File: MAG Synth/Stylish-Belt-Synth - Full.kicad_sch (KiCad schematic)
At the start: 39 parts, among them J0 USB_B, J1 Headphone, J26 WRITE PATCH, J27 PARAM SELECT, J28 PATCH SELECT, J29 MODE, J30 STYLUS, U1 stm32f103c8t6-module-china, U2 XPT8871

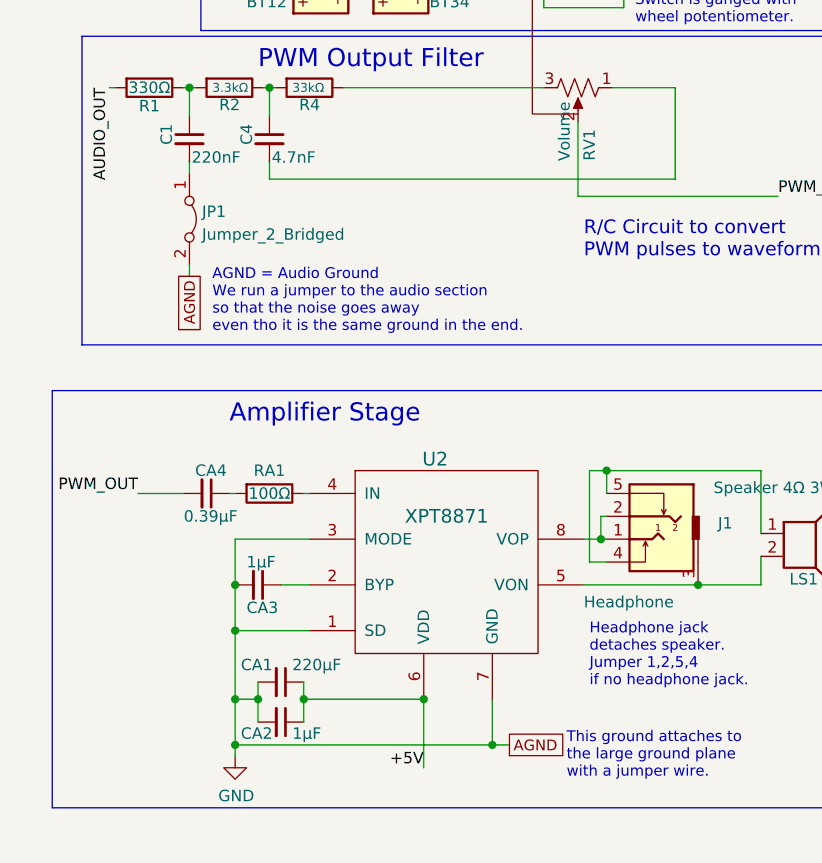
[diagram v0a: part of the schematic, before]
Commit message: Updated fix for audio problems, adds AGND to C4 too. 3d models for parts extracted from old PCB model - only partly complete
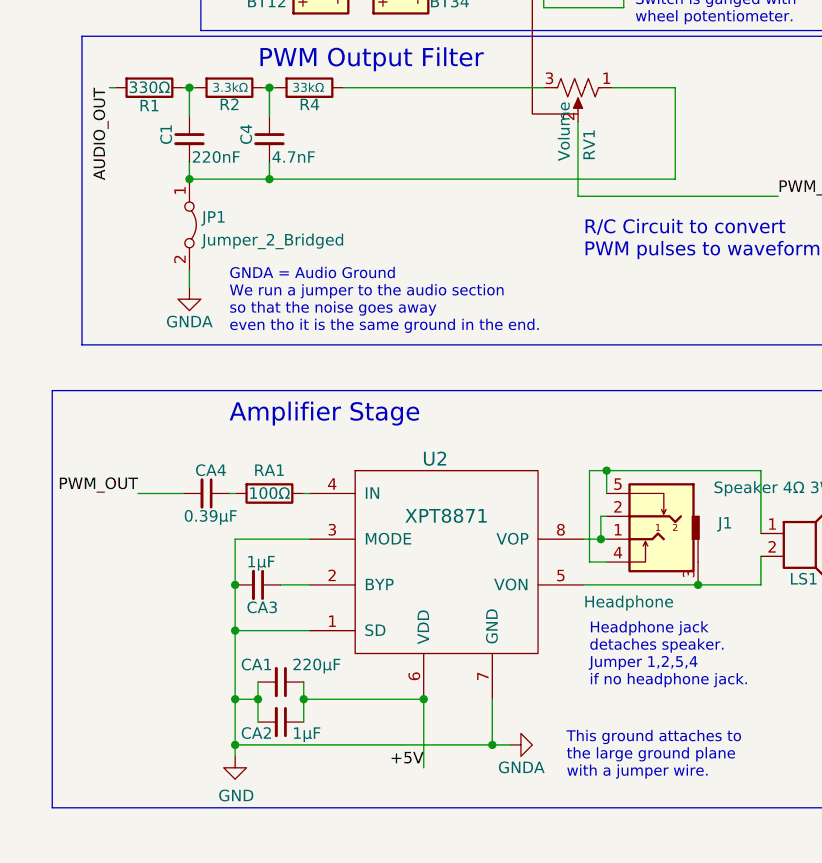
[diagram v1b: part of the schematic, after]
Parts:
- BT12H1, BT34H1: footprint Battery_Holders:BatteryHolder_Keystone_2462_2xAA -> SoftEggKiCAD:BatteryHolder_Keystone_2462_2xAA_MOD
- CA1: footprint SoftEggKiCAD:C_Disc_D5.0mm_W2.5mm_P5.00mm+SMD -> Capacitors_ThroughHole:CP_Radial_Tantal_D4.5mm_P2.50mm
- CA3: footprint Capacitors_ThroughHole:CP_Radial_Tantal_D4.5mm_P2.50mm -> Capacitors_SMD:C_0805_HandSoldering
- R4: footprint SoftEggKiCAD:R_Axial_DIN0204_L3.6mm_D1.6mm_P7.62mm_Horizontal+SMD804 -> SoftEggKiCAD:R_Axial_DIN0204_L3.6mm_D1.6mm_P5mm_Horizontal+SMD804
- U2: footprint SMD_Packages:SOIC-8-N -> SoftEggKiCAD:SOIC-8-N-TP
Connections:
- net at C1.2, JP1.1 (A): now also C4.2, RV1.1
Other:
- note added: "GNDA = Audio Ground We run a jumper to the audio section so that the noise goes away even tho it is the same ground in the end."
- note removed: "AGND = Audio Ground We run a jumper to the audio section so that the noise goes away even tho it is the same ground in the end."
- moved on the sheet: JP1

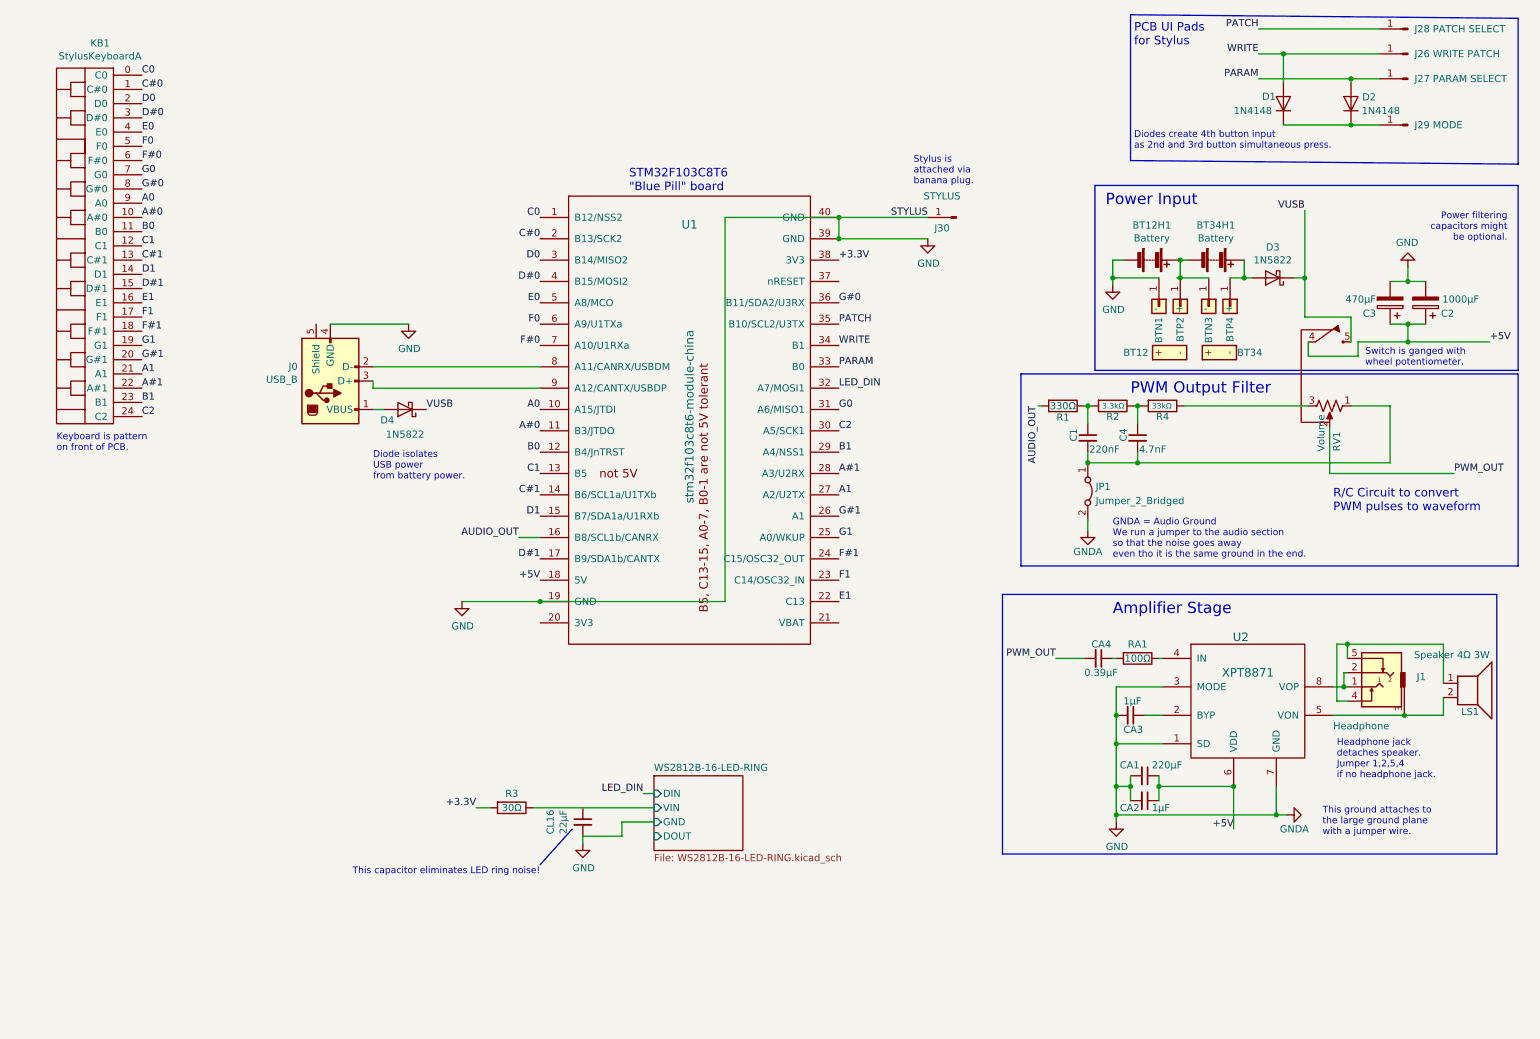
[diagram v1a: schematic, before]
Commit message: Schematic update
All ERC errors resolved.  100+ ERC warnings remain.
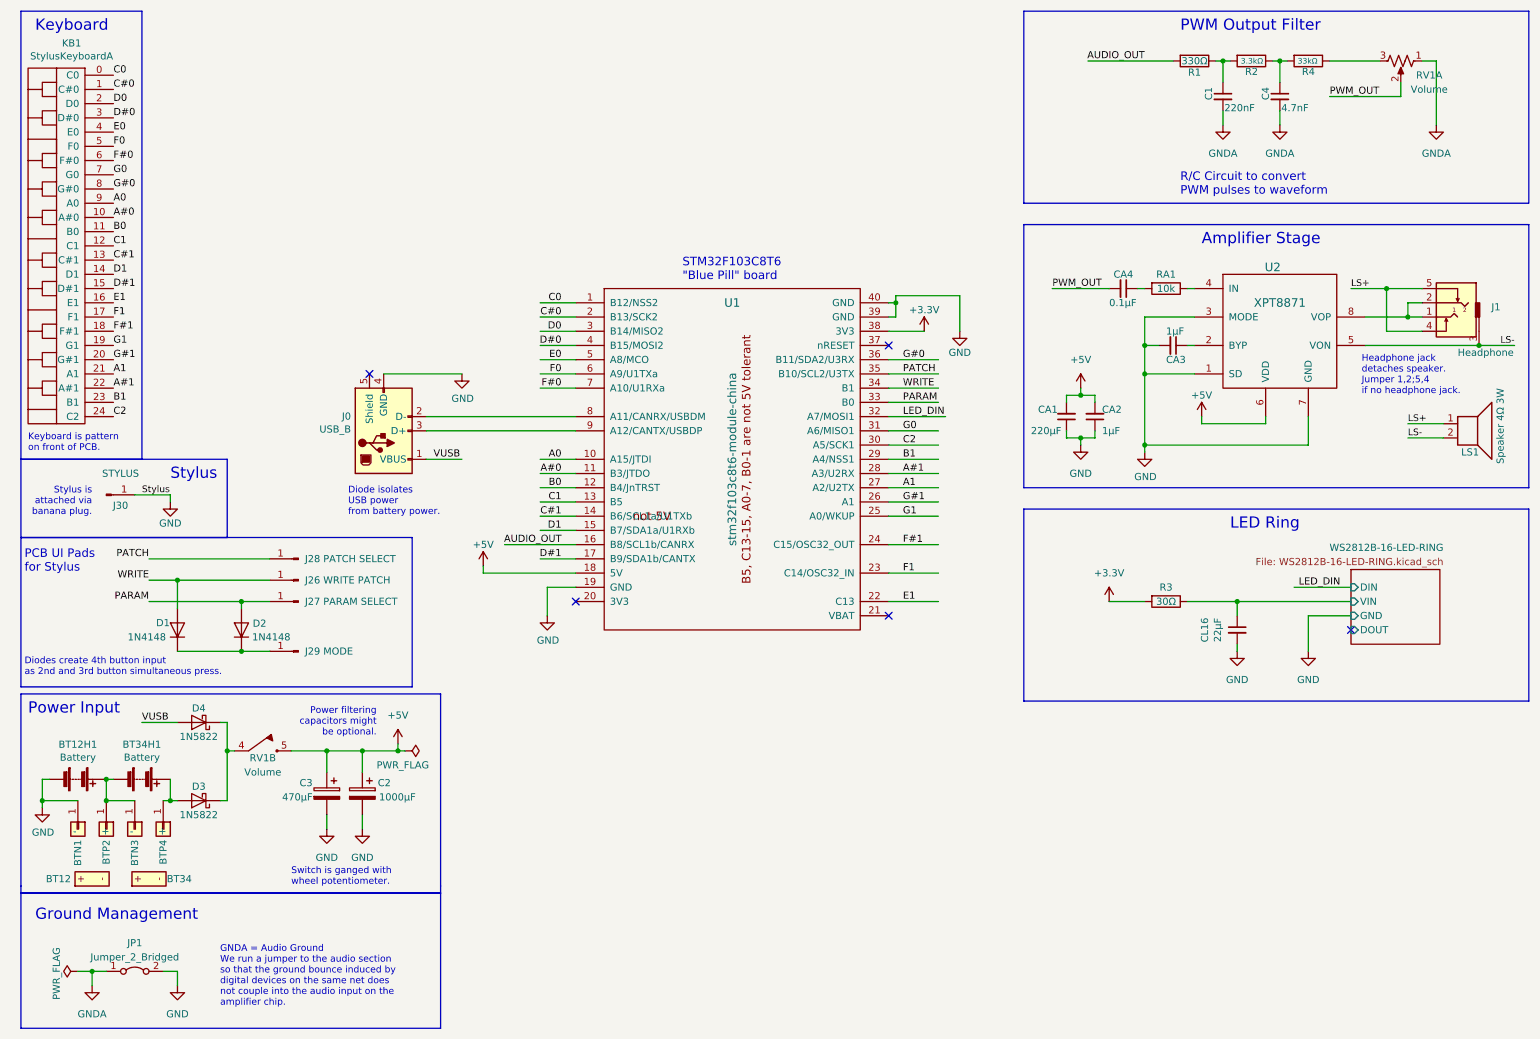
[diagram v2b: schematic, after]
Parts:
- added unit 2 of RV1
- CA4: value 0.39μF -> 0.1μF
- RA1: value 100Ω -> 10k
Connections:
- net +5V: now also CA1.2, CA2.2, RV1.5; no longer CA1.1, CA2.1, RV1.4
- net GND: now also CA1.1, CA2.1; no longer CA1.2, CA2.2
- net VUSB: now also D4.2 (A), J0.1 (VBUS); no longer D3.1 (K), D4.1 (K), RV1.5
- net WS2812B-16-LED-RING/VIN: now also CL16.1
- net GNDA: now reaches C1.2, C4.2, JP1.1 (A), RV1.1
- net LS+: now reaches J1.4, J1.5, LS1.1
- net LS-: now reaches J1.3, LS1.2, U2.5 (VON)
- new net: D3.1 (K), D4.1 (K), RV1.4
- no-connect marks 0 -> 5
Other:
- note added: "GNDA = Audio Ground We run a jumper to the audio section so that the ground bounce induced by digital devices on the same net does not couple into the audio input on the amplifier chip."
- note added: "Ground Management"
- note added: "Headphone jack detaches speaker. Jumper 1,2;5,4 if no headphone jack."
- note added: "Keyboard"
- note added: "LED Ring"
- note added: "Stylus"
- note removed: "GNDA = Audio Ground We run a jumper to the audio section so that the noise goes away even tho it is the same ground in the end."
- note removed: "Headphone jack detaches speaker. Jumper 1,2,5,4 if no headphone jack."
- note removed: "This capacitor eliminates LED ring noise!"
- note removed: "This ground attaches to the large ground plane with a jumper wire."
- moved on the sheet: BT12, BT12H1, BT34, BT34H1, BTN1, BTN3, BTP2, BTP4, C1, C2, C3, C4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

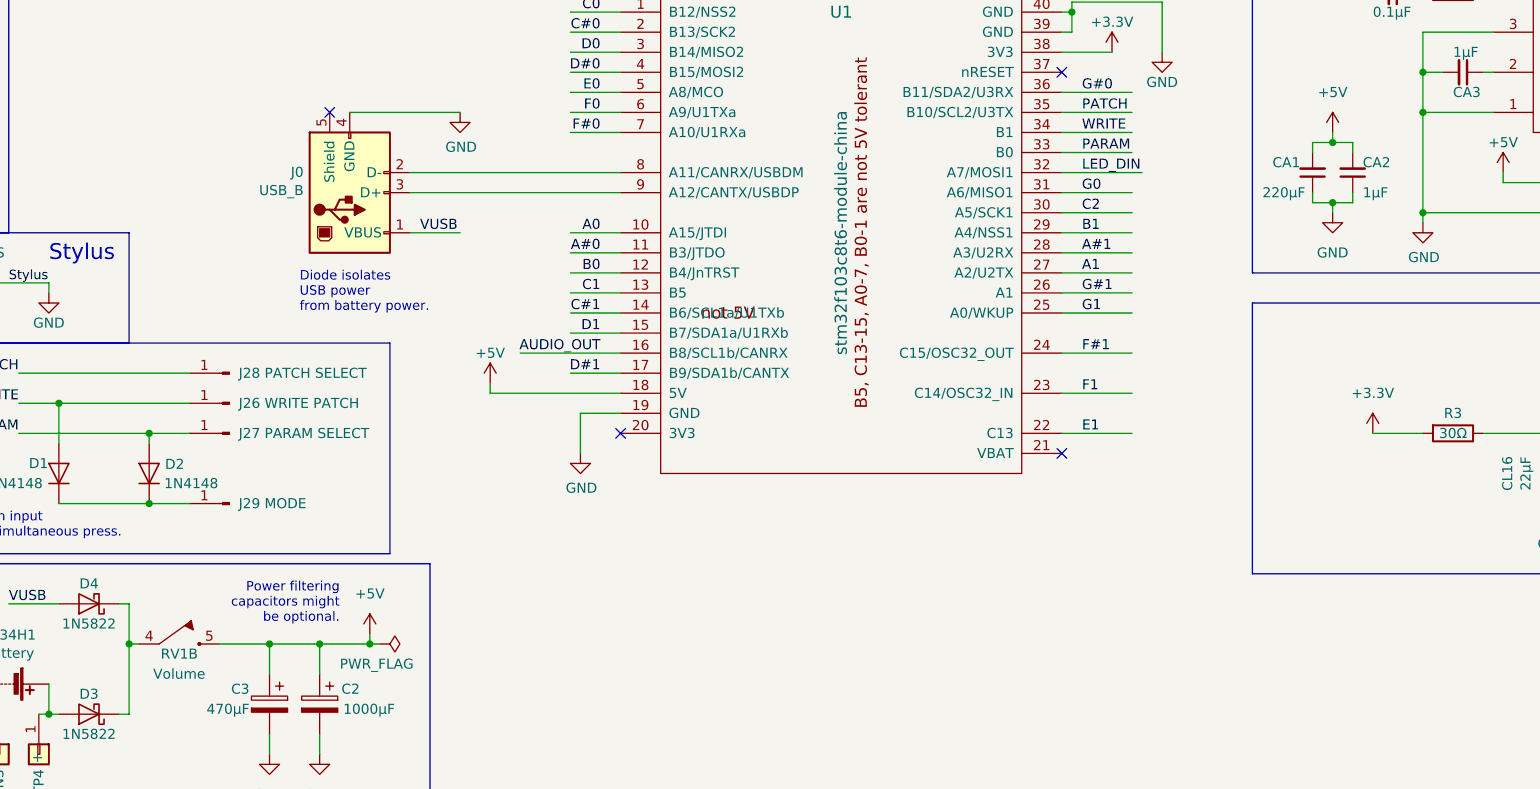
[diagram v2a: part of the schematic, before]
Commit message: Corrected orientation of components to match the PCB again
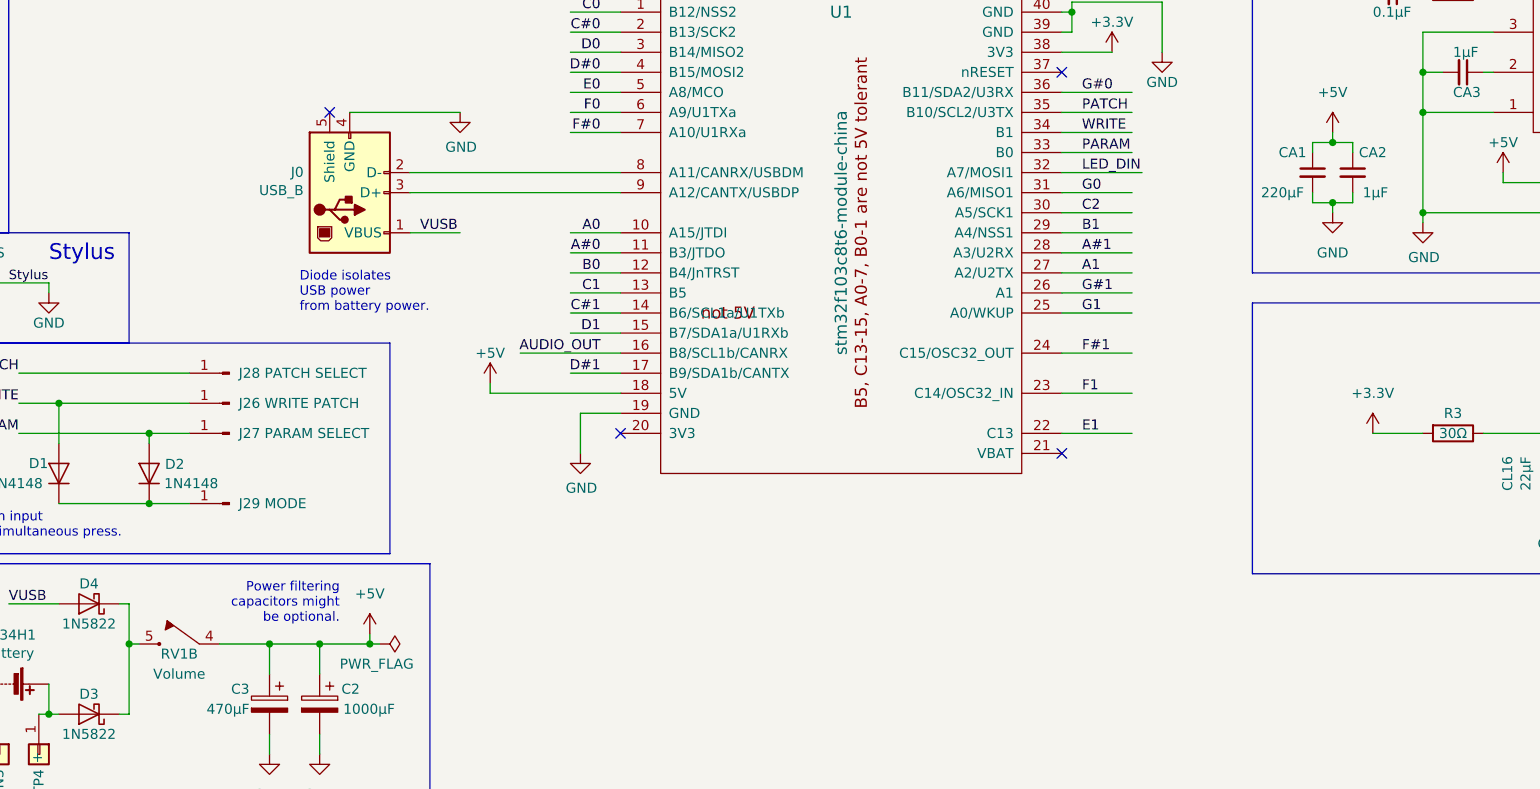
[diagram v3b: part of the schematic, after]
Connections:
- net +5V: now also CA1.1, CA2.1, RV1.4; no longer CA1.2, CA2.2, RV1.5
- net GND: now also CA1.2, CA2.2; no longer CA1.1, CA2.1
- net at D3.1 (K), D4.1 (K): now also RV1.5; no longer RV1.4
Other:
- moved on the sheet: RV1B
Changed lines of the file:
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@@
     )
   )
-  (symbol (lib_id "Stylish-Belt-Synth---Full-rescue:C_Small-device") (at 205.74 86.36 0) (mirror x) (unit 1)
-    (in_bom yes) (on_board yes) (dnp no)
-    (property "Reference" "CA2" (at 207.01 85.09 0)
-      (effects (font (size 1.27 1.27)) (justify left))
+  (symbol (lib_id "Stylish-Belt-Synth---Full-rescue:C_Small-device") (at 205.74 86.36 0) (unit 1)
+    (in_bom yes) (on_board yes) (dnp no)
+    (property "Reference" "CA2" (at 208.28 83.82 0)
+      (effects (font (size 1.27 1.27)))
     )
     (property "Value" "1μF" (at 207.01 88.9 0)
@@
     )
   )
-  (symbol (lib_id "Stylish-Belt-Synth---Full-rescue:C_Small-device") (at 200.66 86.36 0) (mirror x) (unit 1)
-    (in_bom yes) (on_board yes) (dnp no)
-    (property "Reference" "CA1" (at 195.58 85.09 0)
-      (effects (font (size 1.27 1.27)) (justify left))
-    )
-    (property "Value" "220µF" (at 194.31 88.9 0)
-      (effects (font (size 1.27 1.27)) (justify left))
+  (symbol (lib_id "Stylish-Belt-Synth---Full-rescue:C_Small-device") (at 200.66 86.36 0) (unit 1)
+    (in_bom yes) (on_board yes) (dnp no)
+    (property "Reference" "CA1" (at 198.12 83.82 0)
+      (effects (font (size 1.27 1.27)))
+    )
+    (property "Value" "220µF" (at 196.85 88.9 0)
+      (effects (font (size 1.27 1.27)))
     )
     (property "Footprint" "Capacitors_ThroughHole:CP_Radial_Tantal_D4.5mm_P2.50mm" (at 200.66 86.36 0)
@@
     )
   )
-  (symbol (lib_id "SoftEggKicadLib:Switch_Pot") (at 57.15 146.05 270) (unit 2)
+  (symbol (lib_id "SoftEggKicadLib:Switch_Pot") (at 57.15 146.05 90) (mirror x) (unit 2)
     (in_bom yes) (on_board yes) (dnp no)
     (property "Reference" "RV1" (at 57.15 147.32 90)
